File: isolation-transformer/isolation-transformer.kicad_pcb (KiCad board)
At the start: 4 copper layers, 100 x 84 mm, 40 parts, among them J1 Conn_BNC_Vert_PCB, J2 Conn_BNC_Vert_PCB, J3 Conn_BNC_Vert_PCB, J4 Conn_BNC_Vert_PCB, T1 Hammond_560, T2 Hammond_560

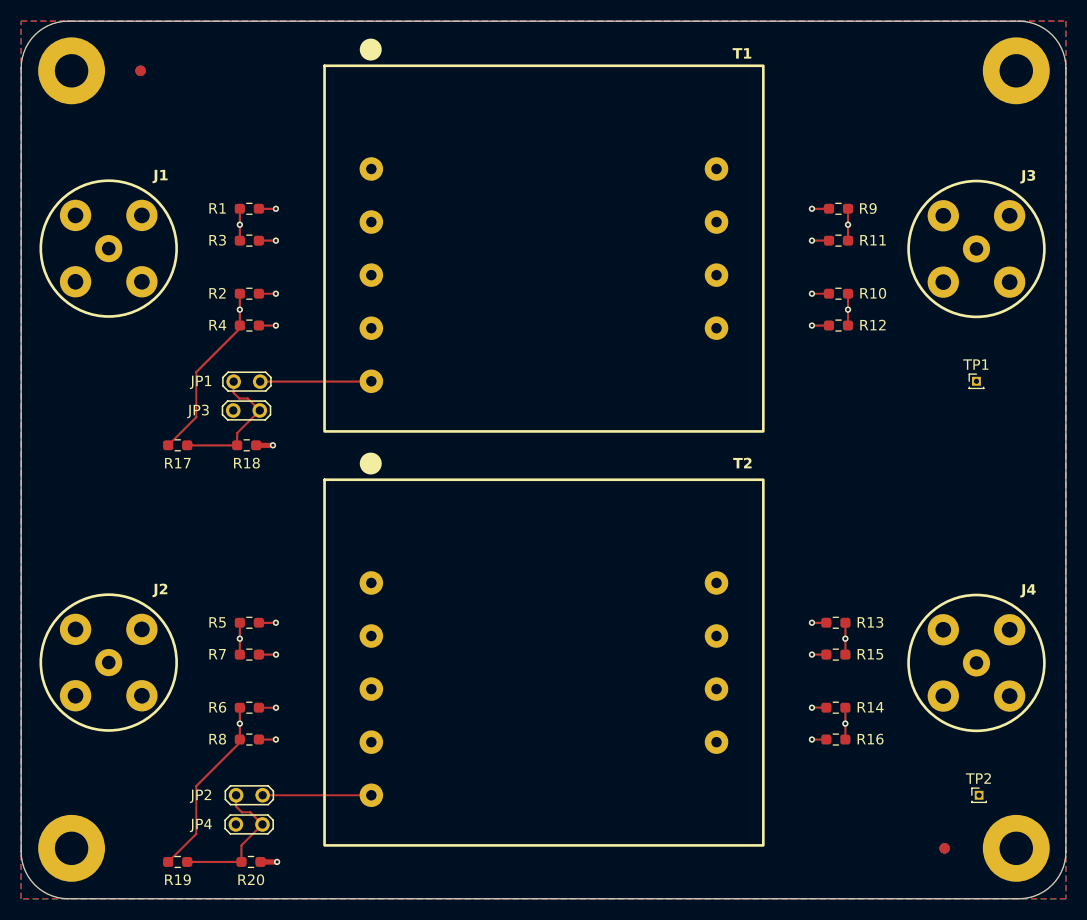
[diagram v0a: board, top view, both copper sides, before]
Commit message: chore: align mtg holes and conns, add perimiter GND vias
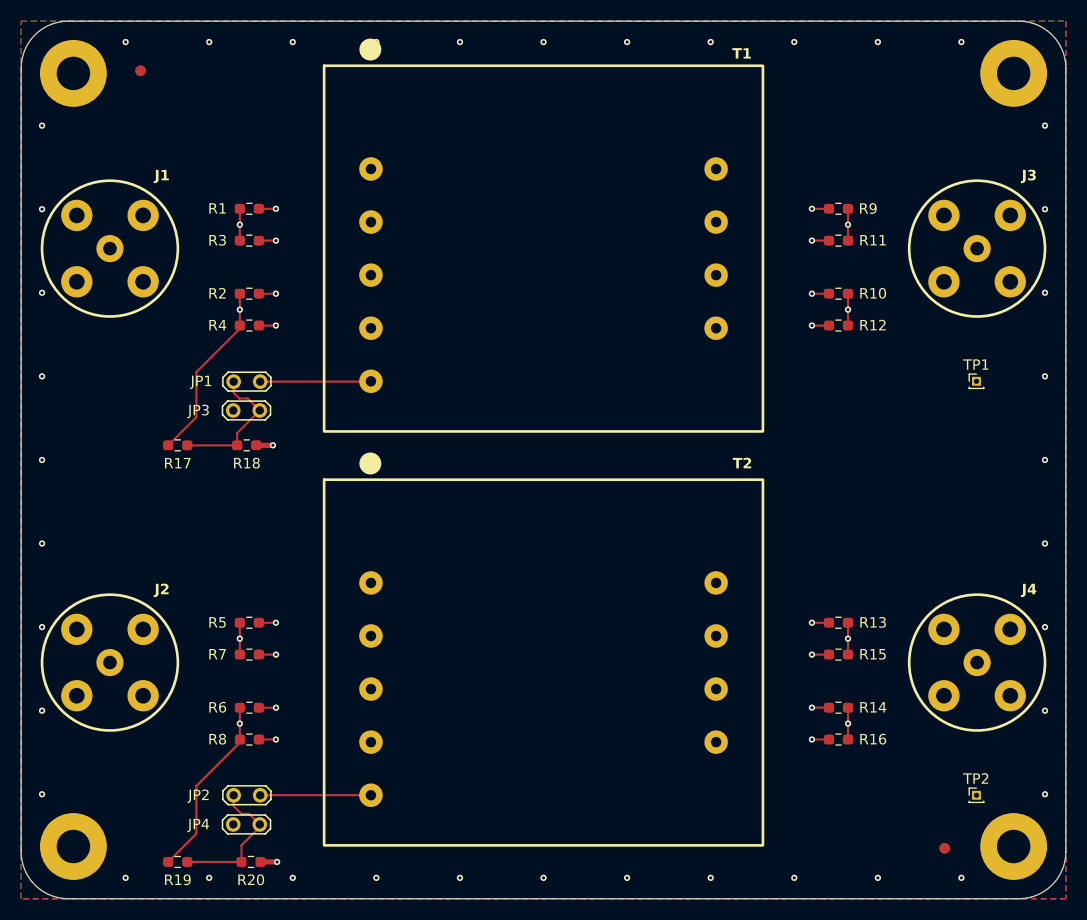
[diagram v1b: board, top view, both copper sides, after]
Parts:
- moved H4 0.35 mm to (190.0, 76.0)
- moved H3 0.30 mm to (190.0, 150.0)
- moved H1 0.30 mm to (100.0, 76.0)
- moved JP4 0.25 mm to (117.8, 147.9)
- moved R13 0.25 mm to (173.2, 128.6)
- moved R14 0.25 mm to (173.2, 136.7)
- moved R15 0.25 mm to (173.2, 131.6)
- moved R16 0.25 mm to (173.2, 139.8)
- moved TP2 0.25 mm to (186.4, 145.1)
- moved H2 0.25 mm to (100.0, 150.0)
- moved JP2 0.23 mm to (115.3, 145.1)
- moved J1 0.12 mm to (103.5, 92.8)
- moved J2 0.12 mm to (103.5, 132.4)
- moved J3 0.07 mm to (186.5, 92.8)
- moved J4 0.07 mm to (186.5, 132.4)
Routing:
- net Net-(J4-Ext): track 39.2 -> 38.7 mm
- net GND: vias 0 -> 40

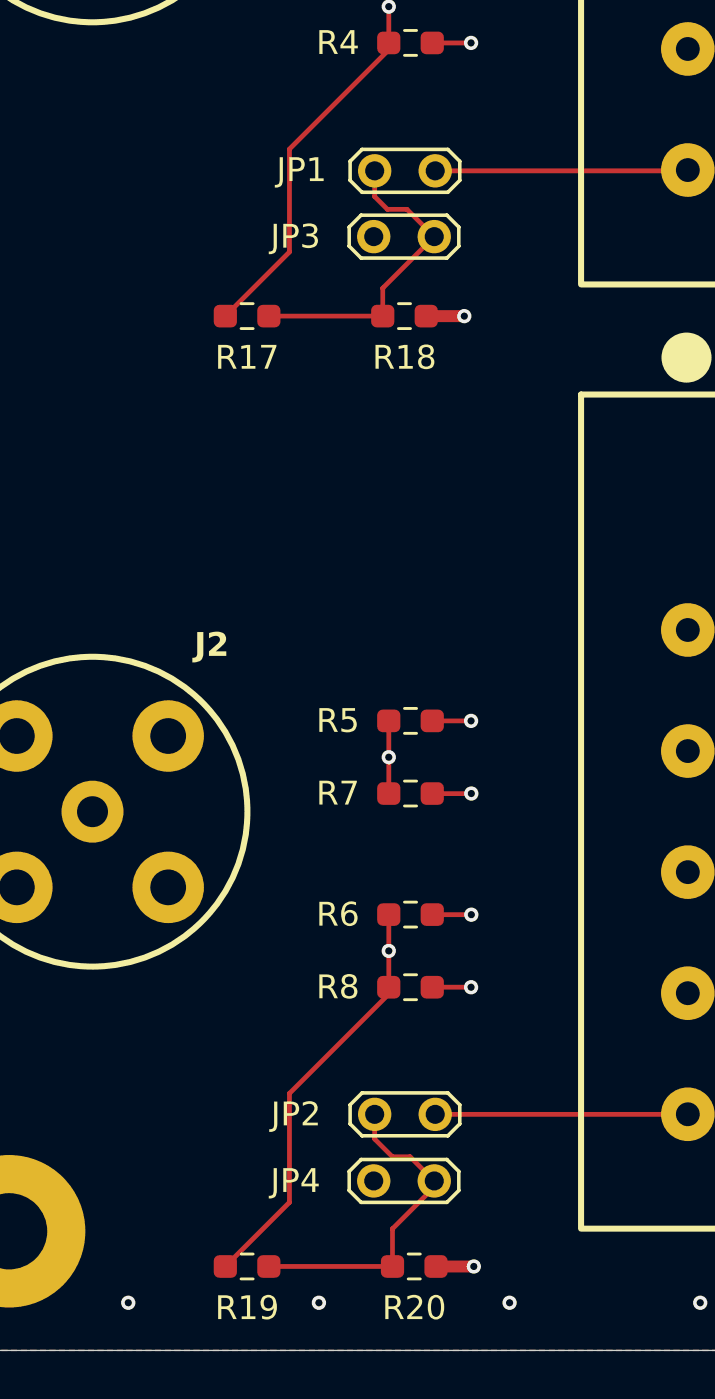
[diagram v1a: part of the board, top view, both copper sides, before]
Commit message: feat: add bypass caps to GND connection
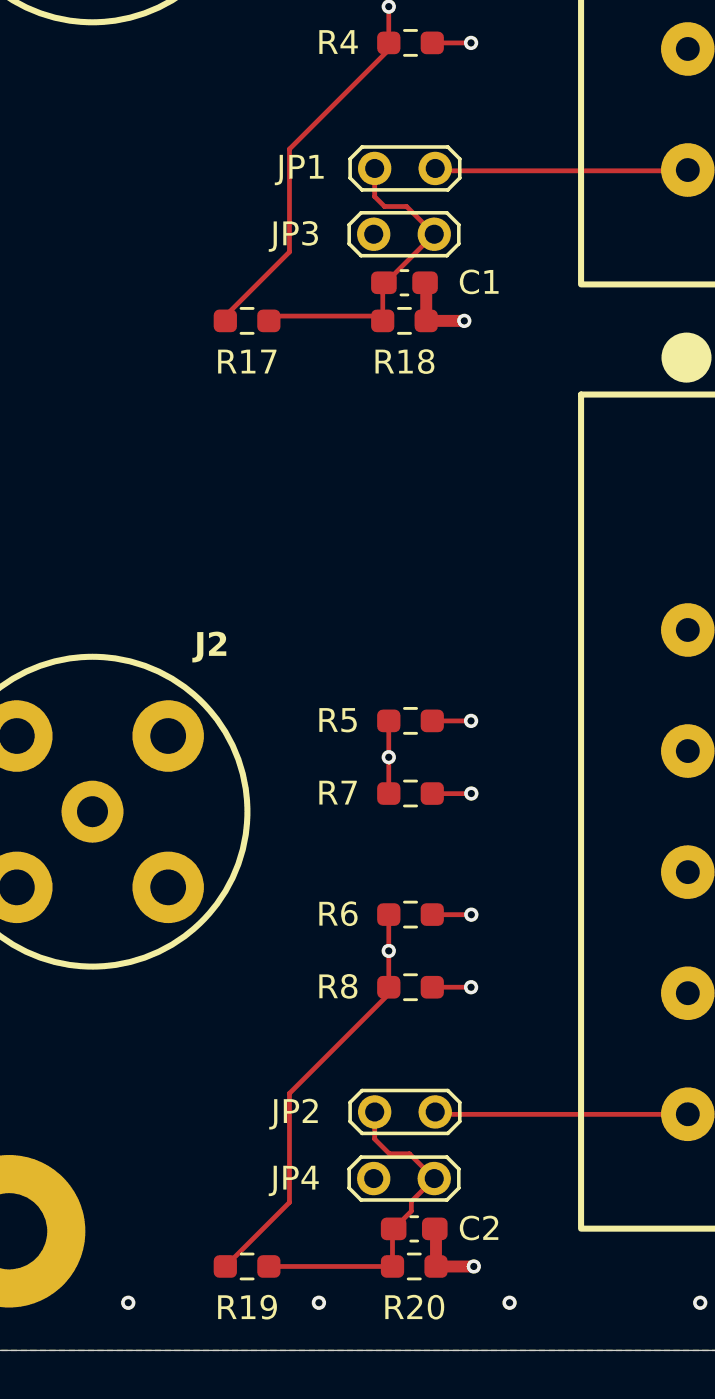
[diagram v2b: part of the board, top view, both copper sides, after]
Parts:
- added C1: C_Small, Capacitor_SMD:C_0603_1608Metric_Pad1.08x0.95mm_HandSolder, F.Cu at (116.6, 110.2)
- added C2: C_Small, Capacitor_SMD:C_0603_1608Metric_Pad1.08x0.95mm_HandSolder, F.Cu at (117.0, 149.9)
- moved R17 0.20 mm to (110.0, 111.8)
- moved R18 0.20 mm to (116.6, 111.8)
- moved JP1 0.10 mm to (115.3, 105.4)
- moved JP2 0.10 mm to (115.3, 145.0)
- moved JP3 0.10 mm to (117.8, 108.2)
- moved JP4 0.10 mm to (117.8, 147.8)
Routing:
- net Net-(C1-Pad2): track 71.5 -> 73.2 mm
- net Net-(C2-Pad2): track 71.2 -> 72.8 mm

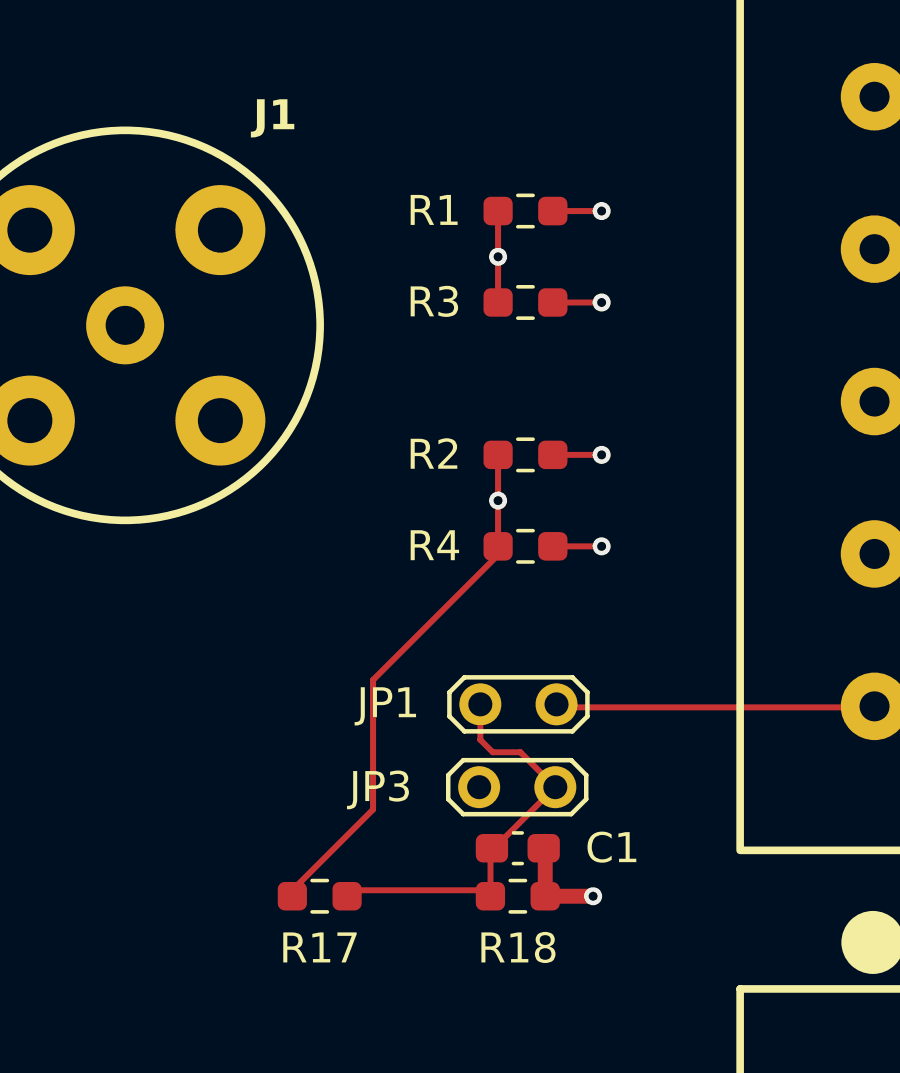
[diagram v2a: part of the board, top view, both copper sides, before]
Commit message: refactor: begin reposition of 0-Ohm links for tighter signal coupling
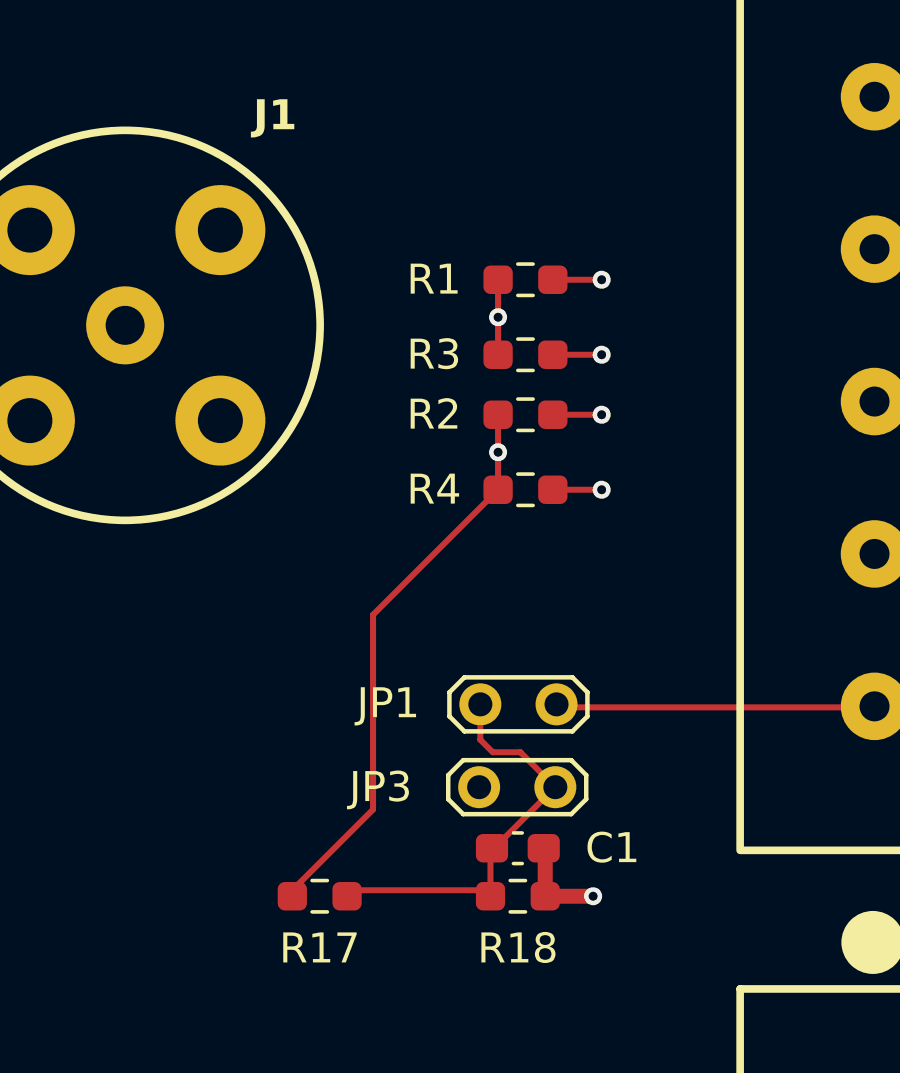
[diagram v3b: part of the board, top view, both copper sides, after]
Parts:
- moved R1 2.29 mm to (116.8, 91.2)
- moved R4 1.89 mm to (116.8, 98.2)
- moved R3 1.74 mm to (116.8, 93.8)
- moved R2 1.34 mm to (116.8, 95.8)
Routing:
- net Net-(J1-In): track 16.8 -> 15.4 mm
- net Net-(T1-IN1A): track 12.4 -> 13.3 mm
- net Net-(R4-Pad2): track 10.9 -> 11.7 mm
- net Net-(T1-IN2A): track 12.2 -> 11.5 mm
- net Net-(J1-Ext): track 53.5 -> 54.1 mm
- net Net-(T1-IN1B): track 13.6 -> 13.1 mm

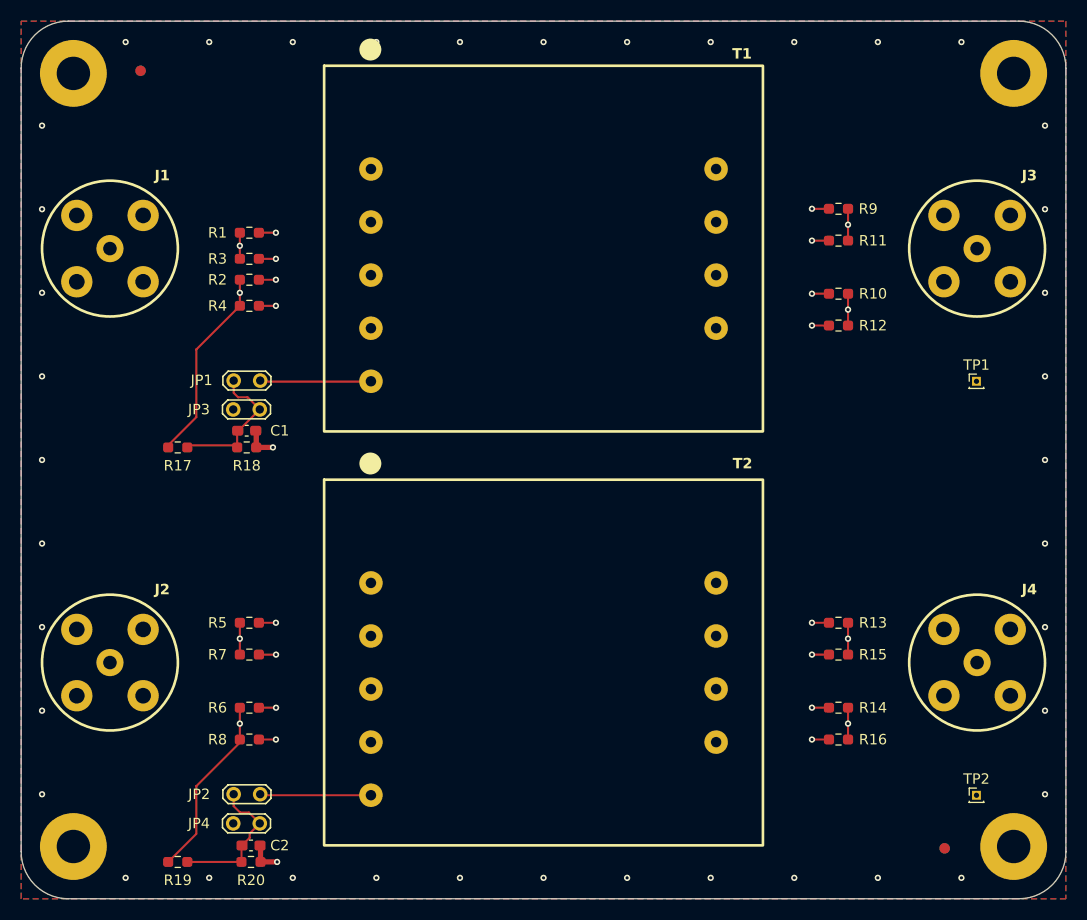
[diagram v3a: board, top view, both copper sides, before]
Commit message: fix (PCB): zero-ohm resistor alignment mismatch between in/out
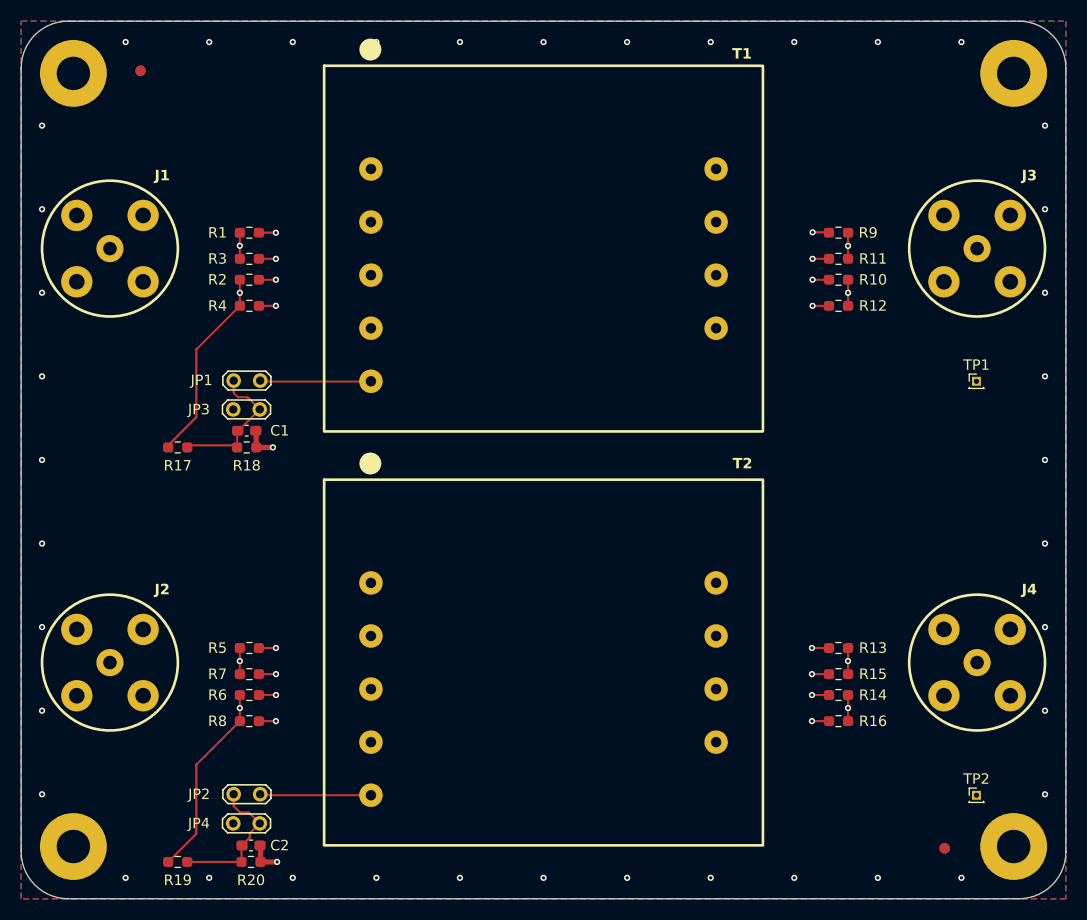
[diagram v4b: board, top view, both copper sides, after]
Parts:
- moved R13 2.42 mm to (173.2, 131.0)
- moved R5 2.42 mm to (116.8, 131.0)
- moved R9 2.29 mm to (173.2, 91.2)
- moved R12 1.89 mm to (173.2, 98.2)
- moved R15 1.87 mm to (173.2, 133.5)
- moved R7 1.87 mm to (116.8, 133.5)
- moved R16 1.76 mm to (173.2, 138.0)
- moved R8 1.76 mm to (116.8, 138.0)
- moved R11 1.74 mm to (173.2, 93.8)
- moved R10 1.34 mm to (173.2, 95.8)
- moved R14 1.21 mm to (173.2, 135.5)
- moved R6 1.21 mm to (116.8, 135.5)
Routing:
- net Net-(J4-In): track 16.6 -> 15.1 mm
- net Net-(J2-In): track 16.6 -> 15.1 mm
- net Net-(J3-In): track 16.3 -> 14.9 mm
- net Net-(T2-OUT1A): track 12.1 -> 13.3 mm
- net Net-(J3-Ext): track 38.7 -> 37.4 mm
- net Net-(T2-IN1A): track 12.4 -> 13.4 mm
- net Net-(T2-OUT2B): track 10.6 -> 11.6 mm
- net Net-(T1-OUT1A): track 12.3 -> 13.3 mm
- net Net-(T1-OUT2B): track 10.9 -> 11.7 mm
- net Net-(T2-IN2A): track 12.2 -> 11.5 mm
- net Net-(R8-Pad2): track 10.9 -> 11.6 mm
- net Net-(T1-OUT2A): track 12.1 -> 11.4 mm
- net Net-(J1-Ext): track 54.1 -> 54.8 mm
- net Net-(J2-Ext): track 53.5 -> 54.1 mm
- net Net-(T1-OUT1B): track 13.6 -> 13.1 mm
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
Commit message: fix (PCB): move L1 traces to L3, update TP footprint
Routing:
- net Net-(J1-Ext): track 54.8 -> 56.2 mm, vias 1 -> 2
- net Net-(J2-Ext): track 54.1 -> 55.4 mm, vias 1 -> 2
